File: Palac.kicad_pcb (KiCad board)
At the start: 2 copper layers, 141.6 x 125.7 mm, 70 parts, among them J2 4PIN, SW1 SW_PUSH, SW10 SW_PUSH, SW11 SW_PUSH, SW12 SW_PUSH, SW13 SW_PUSH, SW14 SW_PUSH, SW15 SW_PUSH, SW16 SW_PUSH, SW17 SW_PUSH, SW18 SW_PUSH, SW19 SW_PUSH, SW2 SW_PUSH, SW20 SW_PUSH, SW21 SW_PUSH, SW22 SW_PUSH, SW23 SW_PUSH, SW24 SW_PUSH, SW25 SW_PUSH, SW26 SW_PUSH, SW27 SW_PUSH, SW28 SW_PUSH, SW29 SW_PUSH, SW3 SW_PUSH, SW30 SW_PUSH, SW4 SW_PUSH, SW5 SW_PUSH, SW6 SW_PUSH, SW7 SW_PUSH, SW8 SW_PUSH, SW9 SW_PUSH, U1 ProMicro

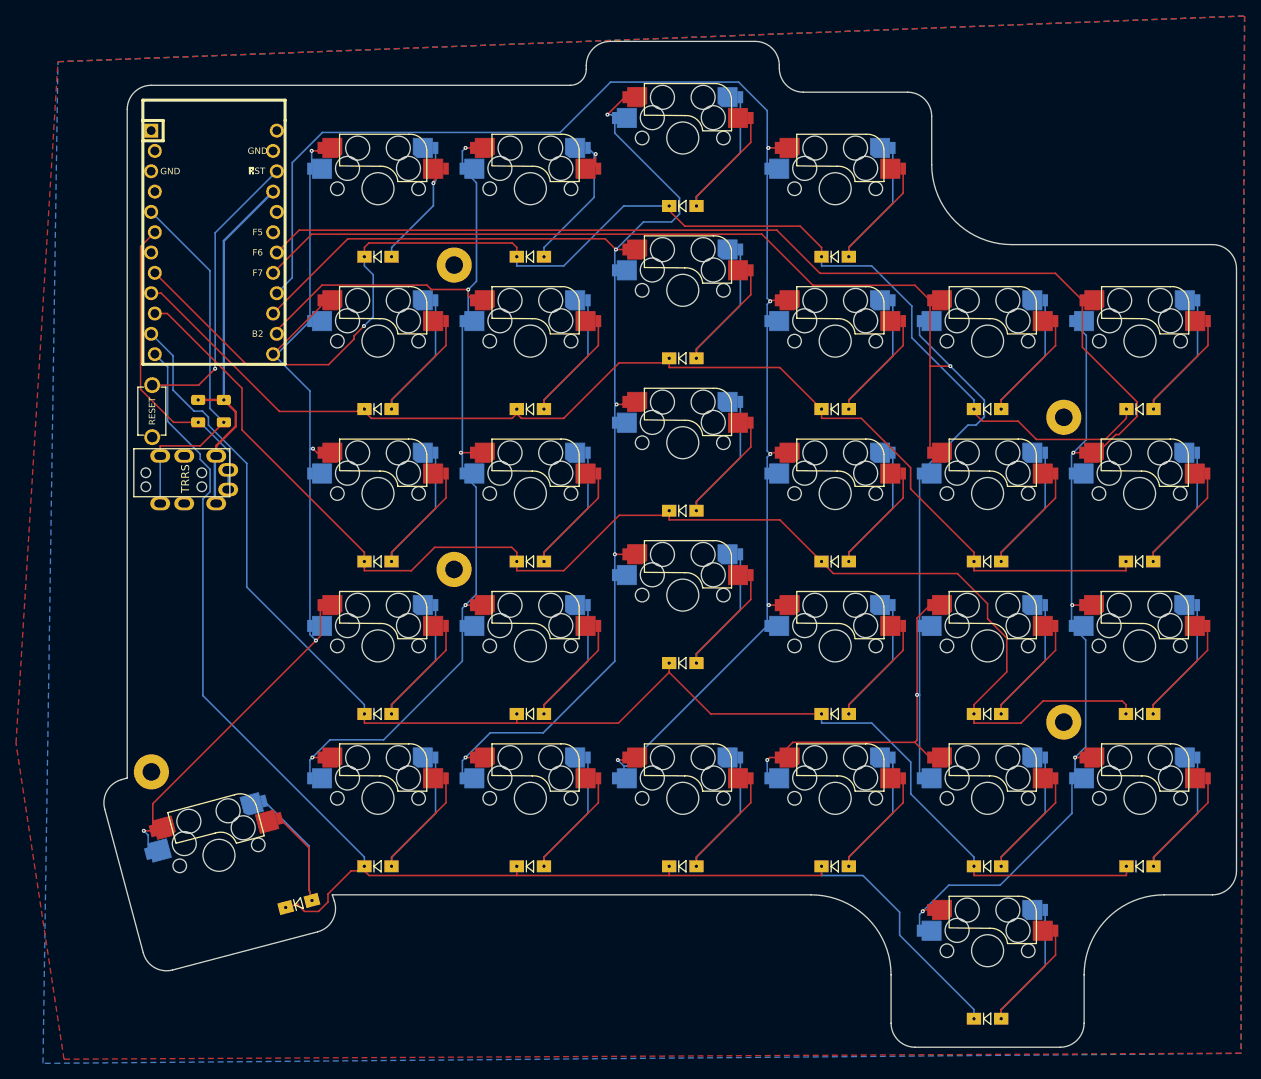
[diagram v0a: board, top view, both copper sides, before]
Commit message: Updated layout
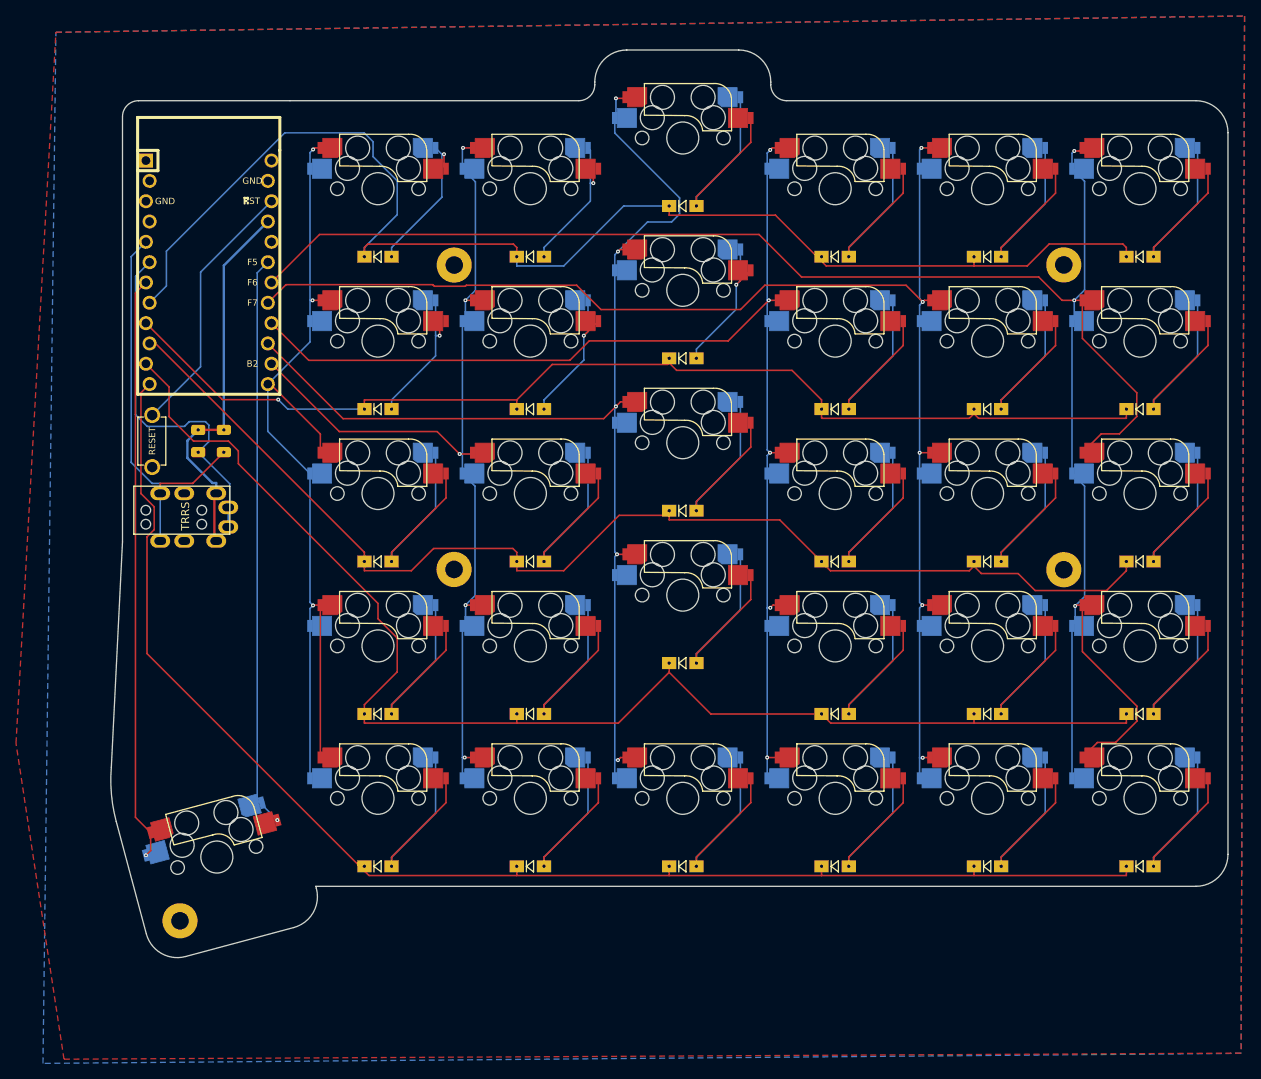
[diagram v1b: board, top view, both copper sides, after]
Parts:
- added SW99: SW_PUSH, Palac:CherryMX_Hotswap, F.Cu at (100.4, 133.5)
- moved D30 26.9 mm to (215.8, 134.7)
- moved SW30 26.9 mm to (215.8, 126.2)
- moved SW25 21.1 mm to (120.5, 126.2), turned to 0 degrees
- moved D18 19.1 mm to (215.8, 96.6)
- moved SW18 19.1 mm to (215.8, 88.1)
- moved D12 19.1 mm to (215.8, 77.5)
- moved SW12 19.1 mm to (215.8, 69.0)
- moved D17 19.1 mm to (196.7, 96.6)
- moved D26 19.1 mm to (139.6, 134.7)
- moved D28 19.1 mm to (177.7, 134.7)
- moved SW17 19.1 mm to (196.7, 88.1)
- moved SW26 19.1 mm to (139.6, 126.2)
- moved SW28 19.1 mm to (177.7, 126.2)
- moved TH4 19.1 mm to (206.2, 59.5)
- moved D11 19.0 mm to (196.7, 77.5)
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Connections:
- U1 pad 19: unconnected-(U1-A2(PF5)-Pad19) -> colT
- U1 pad 7: unconnected-(U1-D4(PD4)-Pad7) -> rowT
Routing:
- net rowT: track 0.00 -> 73.2 mm, vias 0 -> 1
- net colT: track 0.00 -> 71.3 mm, vias 0 -> 1
- net col1: track 216.2 -> 171.4 mm, vias 3 -> 5
- net col2: track 179.4 -> 152.2 mm
- net row2: track 172.5 -> 147.9 mm
- net col0: track 224.2 -> 241.6 mm, vias 4 -> 3
- net Net-(D7-A): track 29.7 -> 17.4 mm, vias 0 -> 1
- net col3: track 159.3 -> 147.6 mm
- net Net-(D9-A): track 29.7 -> 18.4 mm, vias 0 -> 1
- net Net-(D8-A): track 29.7 -> 18.5 mm, vias 0 -> 1
- net col4: track 125.2 -> 114.7 mm
- net row1: track 147.4 -> 137.1 mm, vias 0 -> 1
- net row3: track 176.5 -> 167.3 mm
- net SCL: track 39.0 -> 44.7 mm
- net SDA: track 46.4 -> 51.1 mm
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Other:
- board size 141.6 x 125.7 mm -> 139.6 x 113.5 mm

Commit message: Tidy
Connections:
- net colT renamed SW99
- SW99 pad 1: rowT -> GND
- U1 pad 7: rowT -> unconnected-(U1-D4(PD4)-Pad7)
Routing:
- net rowT: track 73.2 -> 0.00 mm, vias 1 -> 0
- net SW99: track 71.3 -> 71.9 mm
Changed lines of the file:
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@@
   (net 47 "unconnected-(U1-TX(PD3)-Pad1)")
   (net 48 "unconnected-(U1-RX(PD2)-Pad2)")
-  (net 49 "rowT")
-  (net 50 "colT")
-  (net 51 "unconnected-(U1-A3(PF4)-Pad20)")
-  (net 52 "unconnected-(U1-RAW-Pad24)")
+  (net 49 "unconnected-(U1-D4(PD4)-Pad7)")
+  (net 50 "unconnected-(U1-A3(PF4)-Pad20)")
+  (net 51 "unconnected-(U1-RAW-Pad24)")
+  (net 52 "SW99")
   (footprint "Palac:HOLE_M2_TH" (layer "F.Cu")
     (at 130.03 59.542)
@@
       (net 41 "SCL") (pinfunction "SCL(PD0)") (pintype "input"))
     (pad "7" thru_hole circle (at 1.27 7.8486 270) (size 1.7526 1.7526) (drill 1.0922) (layers "*.Cu" "*.SilkS" "*.Mask")
-      (net 49 "rowT") (pinfunction "D4(PD4)") (pintype "input"))
+      (net 49 "unconnected-(U1-D4(PD4)-Pad7)") (pinfunction "D4(PD4)") (pintype "input+no_connect"))
     (pad "8" thru_hole circle (at 3.81 7.3914 270) (size 1.7526 1.7526) (drill 1.0922) (layers "*.Cu" "*.SilkS" "*.Mask")
       (net 5 "row0") (pinfunction "D5(PC6)") (pintype "input"))
@@
       (net 35 "col0") (pinfunction "A1(PF6)") (pintype "input"))
     (pad "19" thru_hole circle (at -1.27 -7.3914 270) (size 1.7526 1.7526) (drill 1.0922) (layers "*.Cu" "*.SilkS" "*.Mask")
-      (net 50 "colT") (pinfunction "A2(PF5)") (pintype "input"))
+      (net 52 "SW99") (pinfunction "A2(PF5)") (pintype "input"))
     (pad "20" thru_hole circle (at -3.81 -7.8486 270) (size 1.7526 1.7526) (drill 1.0922) (layers "*.Cu" "*.SilkS" "*.Mask")
-      (net 51 "unconnected-(U1-A3(PF4)-Pad20)") (pinfunction "A3(PF4)") (pintype "input+no_connect"))
+      (net 50 "unconnected-(U1-A3(PF4)-Pad20)") (pinfunction "A3(PF4)") (pintype "input+no_connect"))
     (pad "21" thru_hole circle (at -6.35 -7.3914 270) (size 1.7526 1.7526) (drill 1.0922) (layers "*.Cu" "*.SilkS" "*.Mask")
       (net 33 "VCC") (pinfunction "VCC") (pintype "input"))
@@
       (net 34 "GND") (pinfunction "GND") (pintype "input"))
     (pad "24" thru_hole circle (at -13.97 -7.8486 270) (size 1.7526 1.7526) (drill 1.0922) (layers "*.Cu" "*.SilkS" "*.Mask")
-      (net 52 "unconnected-(U1-RAW-Pad24)") (pinfunction "RAW") (pintype "input+no_connect"))
+      (net 51 "unconnected-(U1-RAW-Pad24)") (pinfunction "RAW") (pintype "input+no_connect"))
     (model "/home/josef/projekty/keyboards/3d/ARDUINO_PRO_MICRO_cp.wrl"
       (offset (xyz 0 0 0))
@@
     (pad "" np_thru_hole circle (at 5.08 0 15) (size 1.7 1.7) (drill 1.7) (layers "*.Cu" "*.Mask"))
     (pad "1" smd custom (at -8.5 -2.5 15) (size 0.7 1.5) (layers "B.Cu" "B.Paste" "B.Mask")
-      (net 49 "rowT") (pinfunction "1") (pintype "passive") (thermal_bridge_angle 45)
+      (net 34 "GND") (pinfunction "1") (pintype "passive") (thermal_bridge_angle 45)
       (options (clearance outline) (anchor rect))
       (primitives
@@
       ))
     (pad "1" smd custom (at -7.2 -5.1 15) (size 0.7 1.5) (layers "F.Cu" "F.Paste" "F.Mask")
-      (net 49 "rowT") (pinfunction "1") (pintype "passive") (thermal_bridge_angle 45)
+      (net 34 "GND") (pinfunction "1") (pintype "passive") (thermal_bridge_angle 45)
       (options (clearance outline) (anchor rect))
       (primitives
@@
       ))
     (pad "2" smd custom (at 7.2 -5.1 15) (size 0.7 1.5) (layers "B.Cu" "B.Paste" "B.Mask")
-      (net 50 "colT") (pinfunction "2") (pintype "passive") (thermal_bridge_angle 45)
+      (net 52 "SW99") (pinfunction "2") (pintype "passive") (thermal_bridge_angle 45)
       (options (clearance outline) (anchor rect))
       (primitives
@@
       ))
     (pad "2" smd custom (at 8.5 -2.5 15) (size 0.7 1.5) (layers "F.Cu" "F.Paste" "F.Mask")
-      (net 50 "colT") (pinfunction "2") (pintype "passive") (thermal_bridge_angle 45)
+      (net 52 "SW99") (pinfunction "2") (pintype "passive") (thermal_bridge_angle 45)
       (options (clearance outline) (anchor rect))
       (primitives
@@
   (segment (start 217.45 134.7) (end 217.45 133.5497) (width 0.2) (layer "B.Cu") (net 46))
   (segment (start 222.95 128.0497) (end 222.95 121.1) (width 0.2) (layer "B.Cu") (net 46))
-  (segment (start 92.083157 130.477875) (end 92.083157 132.743243) (width 0.2) (layer "F.Cu") (net 49))
-  (segment (start 90.1781 128.572818) (end 92.083157 130.477875) (width 0.2) (layer "F.Cu") (net 49))
-  (segment (start 90.1781 63.0366) (end 90.1781 128.572818) (width 0.2) (layer "F.Cu") (net 49))
-  (segment (start 92.083157 132.743243) (end 91.5004 133.326) (width 0.2) (layer "F.Cu") (net 49))
-  (segment (start 91.4932 61.7215) (end 90.1781 63.0366) (width 0.2) (layer "F.Cu") (net 49))
-  (via (at 91.5004 133.326) (size 0.5) (drill 0.2) (layers "F.Cu" "B.Cu") (net 49))
-  (via (at 107.921 128.926) (size 0.5) (drill 0.2) (layers "F.Cu" "B.Cu") (net 50))
-  (segment (start 107.921 128.926) (end 105.4032 126.4082) (width 0.2) (layer "B.Cu") (net 50))
-  (segment (start 105.4032 126.4082) (end 105.4032 60.5115) (width 0.2) (layer "B.Cu") (net 50))
-  (segment (start 105.4032 60.5115) (end 106.7332 59.1815) (width 0.2) (layer "B.Cu") (net 50))
+  (via (at 107.921 128.926) (size 0.5) (drill 0.2) (layers "F.Cu" "B.Cu") (net 52))
+  (segment (start 106.7332 59.1815) (end 105.4569 60.4578) (width 0.2) (layer "B.Cu") (net 52))
+  (segment (start 107.921 128.926) (end 105.4032 126.4082) (width 0.2) (layer "B.Cu") (net 52))
+  (segment (start 105.4569 126.215292) (end 105.992489 126.750881) (width 0.2) (layer "B.Cu") (net 52))
+  (segment (start 105.4569 60.4578) (end 105.4569 126.215292) (width 0.2) (layer "B.Cu") (net 52))
   (zone (net 34) (net_name "GND") (layer "F.Cu") (hatch edge 0.508)
     (connect_pads (clearance 0.508))
